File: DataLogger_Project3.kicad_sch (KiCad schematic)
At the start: 24 parts, among them U1 24LC1025, U2 24LC1025, U3 DS1337S_, U4 ATMEGA328P-AU, Y1 Crystal

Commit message: added values
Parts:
- added Y2: 16Mhz, symbol Device:Crystal
- C1, C2: value C -> 22pF
- C3, C4: value C -> 0.1uF
- C5: value C_Polarized -> 100nF
- R1, R5: value R -> 330ohm
- R2, R3, R4: value R -> 10k
- R6, R7: value R -> 4.7k
- Y1: value Crystal -> 32.768kHz
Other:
- moved on the sheet: BT1, C1, C2, C3, C4, C5, D1, D2, H1, H2, H3, H4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

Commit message: added footprints
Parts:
- BT1: footprint (none) -> Connector_PinHeader_2.54mm:PinHeader_1x02_P2.54mm_Vertical
- C1, C2, C3, C4, C5: footprint (none) -> Capacitor_SMD:C_0805_2012Metric
- D1, D2: footprint (none) -> LED_SMD:LED_0805_2012Metric
- H1, H2, H3, H4: footprint (none) -> MountingHole:MountingHole_2.1mm
- R1, R2, R3, R4, R5, R6, R7: footprint (none) -> Resistor_SMD:R_0805_2012Metric
- U1, U2: footprint (none) -> Package_SO:SOIC-8_5.3x5.3mm_P1.27mm
- U3: footprint DS1337S_:SOIC127P600X175-8N -> Footprints:SOIC127P600X175-8N
- U4: footprint ATMEGA328P-AU:QFP80P900X900X120-32N -> Footprints:QFP80P900X900X120-32N
- Y1, Y2: footprint (none) -> Crystal:Crystal_SMD_5032-2Pin_5.0x3.2mm_HandSoldering
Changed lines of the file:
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@@
 			)
 		)
-		(property "Footprint" ""
+		(property "Footprint" "Capacitor_SMD:C_0805_2012Metric"
 			(at 183.8452 62.23 0)
 			(effects
@@
 			)
 		)
-		(property "Footprint" ""
+		(property "Footprint" "Resistor_SMD:R_0805_2012Metric"
 			(at 183.642 91.44 90)
 			(effects
@@
 			)
 		)
-		(property "Footprint" ""
+		(property "Footprint" "Package_SO:SOIC-8_5.3x5.3mm_P1.27mm"
 			(at 86.36 162.56 0)
 			(effects
@@
 			)
 		)
-		(property "Footprint" ""
+		(property "Footprint" "LED_SMD:LED_0805_2012Metric"
 			(at 204.47 48.26 0)
 			(effects
@@
 			)
 		)
-		(property "Footprint" ""
+		(property "Footprint" "Capacitor_SMD:C_0805_2012Metric"
 			(at 254.9652 34.29 0)
 			(effects
@@
 			)
 		)
-		(property "Footprint" ""
+		(property "Footprint" "Resistor_SMD:R_0805_2012Metric"
 			(at 82.042 52.07 90)
 			(effects
@@
 			)
 		)
-		(property "Footprint" ""
+		(property "Footprint" "MountingHole:MountingHole_2.1mm"
 			(at 243.84 129.54 0)
 			(effects
@@
 			)
 		)
-		(property "Footprint" ""
+		(property "Footprint" "Connector_PinHeader_2.54mm:PinHeader_1x02_P2.54mm_Vertical"
 			(at 269.24 26.416 90)
 			(effects
@@
 			)
 		)
-		(property "Footprint" ""
+		(property "Footprint" "MountingHole:MountingHole_2.1mm"
 			(at 243.84 119.38 0)
 			(effects
@@
 			)
 		)
-		(property "Footprint" ""
+		(property "Footprint" "MountingHole:MountingHole_2.1mm"
 			(at 243.84 144.78 0)
 			(effects
@@
 			)
 		)
-		(property "Footprint" ""
+		(property "Footprint" "Resistor_SMD:R_0805_2012Metric"
 			(at 102.362 163.83 90)
 			(effects
@@
 			)
 		)
-		(property "Footprint" ""
+		(property "Footprint" "Resistor_SMD:R_0805_2012Metric"
 			(at 82.042 64.77 90)
 			(effects
@@
 			)
 		)
-		(property "Footprint" "ATMEGA328P-AU:QFP80P900X900X120-32N"
+		(property "Footprint" "Footprints:QFP80P900X900X120-32N"
 			(at 228.6 66.04 0)
 			(effects
@@
 			)
 		)
-		(property "Footprint" ""
+		(property "Footprint" "LED_SMD:LED_0805_2012Metric"
 			(at 266.7 48.26 0)
 			(effects
@@
 			)
 		)
-		(property "Footprint" ""
+		(property "Footprint" "Resistor_SMD:R_0805_2012Metric"
 			(at 117.602 163.83 90)
 			(effects
@@
 			)
 		)
-		(property "Footprint" ""
+		(property "Footprint" "Resistor_SMD:R_0805_2012Metric"
 			(at 183.642 45.72 90)
 			(effects
@@
 			)
 		)
-		(property "Footprint" ""
+		(property "Footprint" "Package_SO:SOIC-8_5.3x5.3mm_P1.27mm"
 			(at 53.34 162.56 0)
 			(effects
@@
 			)
 		)
-		(property "Footprint" ""
+		(property "Footprint" "Capacitor_SMD:C_0805_2012Metric"
 			(at 204.1652 95.25 0)
 			(effects
@@
 			)
 		)
-		(property "Footprint" ""
+		(property "Footprint" "Crystal:Crystal_SMD_5032-2Pin_5.0x3.2mm_HandSoldering"
 			(at 201.93 63.5 0)
 			(effects
@@
 			)
 		)
-		(property "Footprint" ""
+		(property "Footprint" "Crystal:Crystal_SMD_5032-2Pin_5.0x3.2mm_HandSoldering"
 			(at 27.94 50.8 0)
 			(effects
@@
 			)
 		)
-		(property "Footprint" "DS1337S_:SOIC127P600X175-8N"
+		(property "Footprint" "Footprints:SOIC127P600X175-8N"
 			(at 55.88 50.8 0)
 			(effects
@@
 			)
 		)
-		(property "Footprint" ""
+		(property "Footprint" "MountingHole:MountingHole_2.1mm"
 			(at 243.84 137.16 0)
 			(effects
@@
 			)
 		)
-		(property "Footprint" ""
+		(property "Footprint" "Capacitor_SMD:C_0805_2012Metric"
 			(at 191.4652 80.01 0)
 			(effects
@@
 			)
 		)
-		(property "Footprint" ""
+		(property "Footprint" "Resistor_SMD:R_0805_2012Metric"
 			(at 264.922 64.77 90)
 			(effects
@@
 			)
 		)
-		(property "Footprint" ""
+		(property "Footprint" "Capacitor_SMD:C_0805_2012Metric"
 			(at 97.4852 59.69 0)
 			(effects

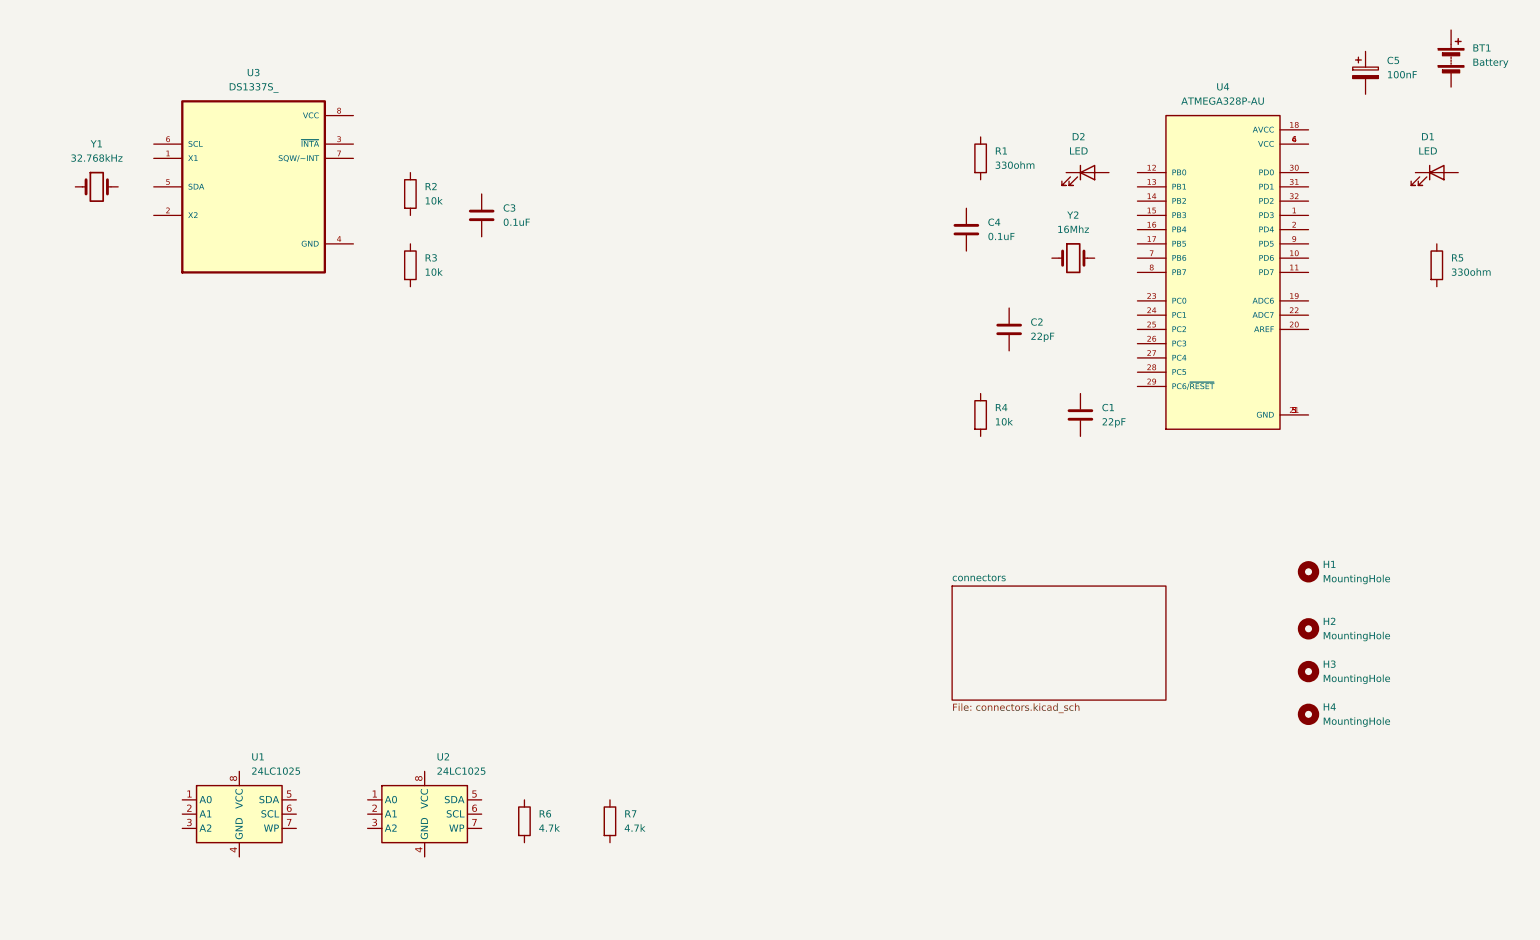
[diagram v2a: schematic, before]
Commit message: wired the components
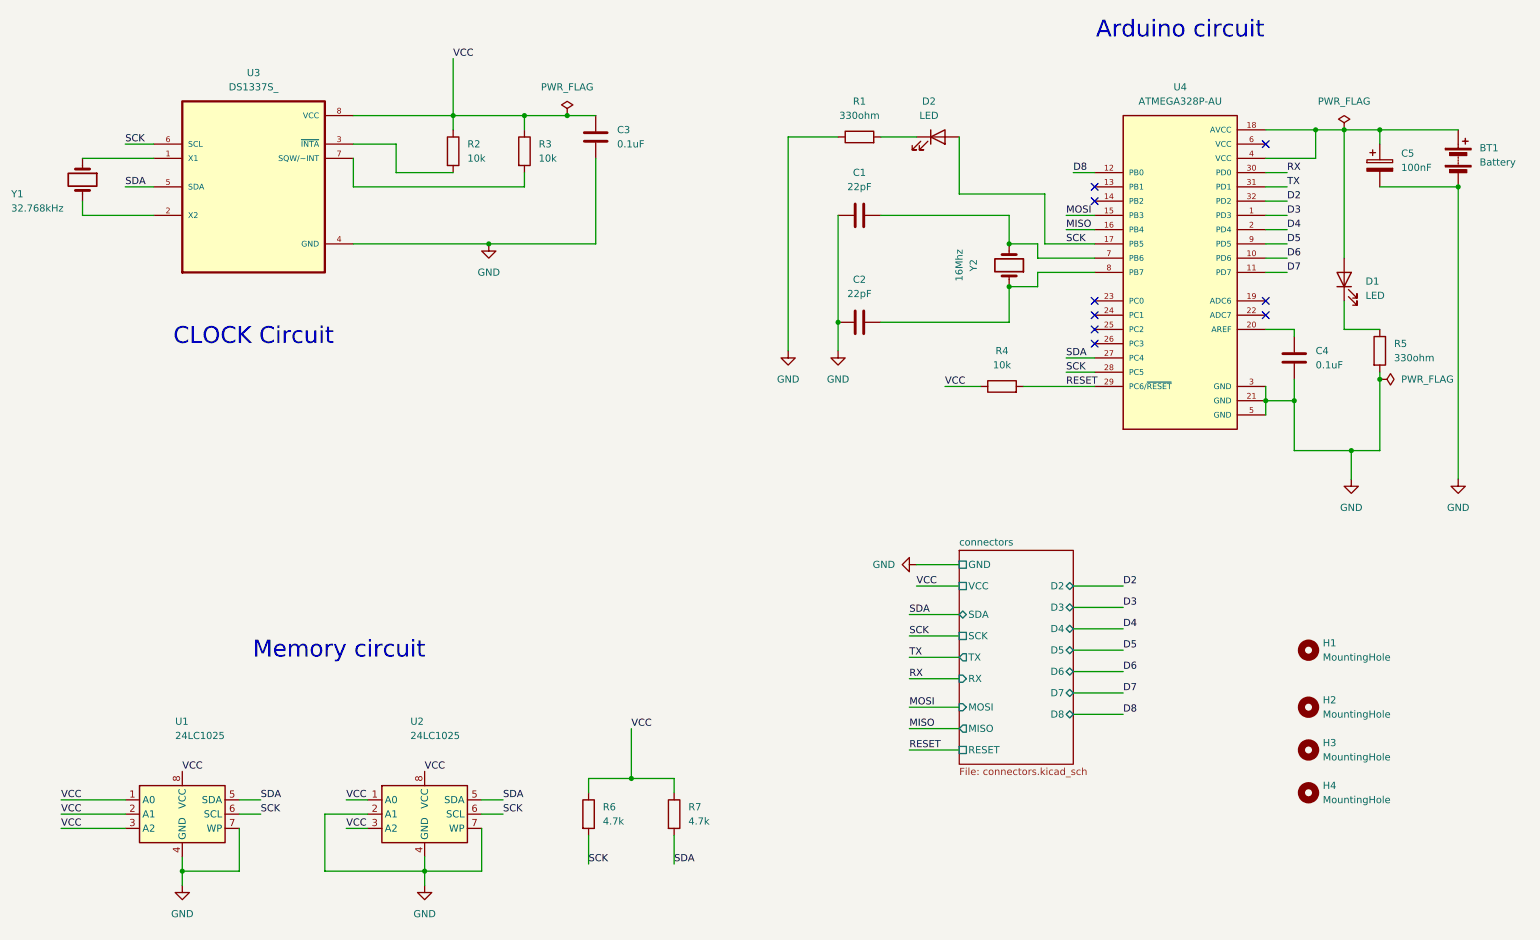
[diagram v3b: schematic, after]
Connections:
- net GND: now reaches C4.1
- net GND: now also BT1.2 (-), C1.1, C2.1, C3.2, C5.2, R1.1, R5.2, U1.4 (GND), U1.7 (WP), U2.2 (A1), U2.4 (GND), U2.7 (WP), U3.4 (GND), U4.21 (GND), U4.3 (GND), U4.5 (GND)
- net at C4.2: now also U4.20 (AREF)
- net VCC: now reaches R4.1
- net VCC: now also C3.1, R2.1, R3.1, R6.1, R7.1, U1.1 (A0), U1.2 (A1), U1.3 (A2), U1.8 (VCC), U2.1 (A0), U2.3 (A2), U2.8 (VCC), U3.8 (VCC)
- net RESET: now reaches R4.2
- net RESET: now also U4.29 (PC6/~{RESET})
- net SDA: now reaches U2.5 (SDA)
- net SDA: now also R7.2, U1.5 (SDA), U3.5 (SDA), U4.27 (PC4)
- net SCK: now reaches U2.6 (SCL)
- net SCK: now also D2.2 (A), R6.2, U1.6 (SCL), U3.6 (SCL), U4.17 (PB5), U4.28 (PC5)
- net at D2.1 (K): now also R1.2
- net at C5.1: now also BT1.1 (+), D1.2 (A), U4.18 (AVCC), U4.4 (VCC)
- net at R2.2: now also U3.3 (~{INTA})
- net at R3.2: now also U3.7 (SQW/~INT)
- net D3: now reaches U4.1 (PD3)
- net D6: now reaches U4.10 (PD6)
- net D7: now reaches U4.11 (PD7)
- net D8: now reaches U4.12 (PB0)
- net MOSI: now reaches U4.15 (PB3)
- net MISO: now reaches U4.16 (PB4)
- net D4: now reaches U4.2 (PD4)
- net RX: now reaches U4.30 (PD0)
- net TX: now reaches U4.31 (PD1)
- net D2: now reaches U4.32 (PD2)
- net at U4.6 (VCC): no longer U4.4 (VCC)
- net at U4.7 (PB6): now also C1.2, Y2.2
- net at U4.8 (PB7): now also C2.2, Y2.1
- net D5: now reaches U4.9 (PD5)
- net at D1.1 (K): now also R5.1
- net at Y1.1: now also U3.1 (X1)
- net at Y1.2: now also U3.2 (X2)
- no-connect marks 0 -> 9
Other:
- sheet connectors ports: added D2, D3, D4, D5, D6, D7, D8, GND, MISO, MOSI, RESET, RX, SCK, SDA, TX, VCC; removed none
- note added: "Arduino circuit"
- note added: "CLOCK Circuit"
- note added: "Memory circuit"
- moved on the sheet: BT1, C1, C2, C3, C4, C5, D1, D2, H1, H2, H3, H4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
